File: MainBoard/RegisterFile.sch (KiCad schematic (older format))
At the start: 4 parts, among them U53 IDT7024L15PFG, U54 IDT7024L15PFG

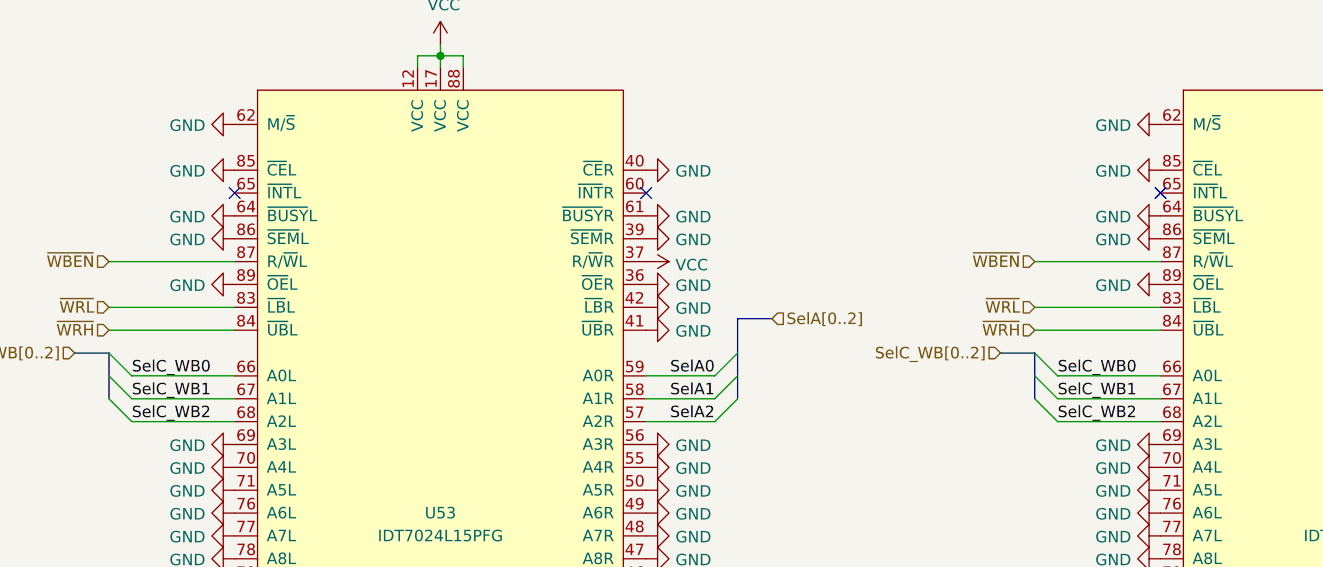
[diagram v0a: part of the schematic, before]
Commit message: Fix incorrectly wired control signals in register file write port.
The left sides of the register file's two dual port SRAMs were being set to
output their values. We never want these ports to output their values. This
is the register file write port.
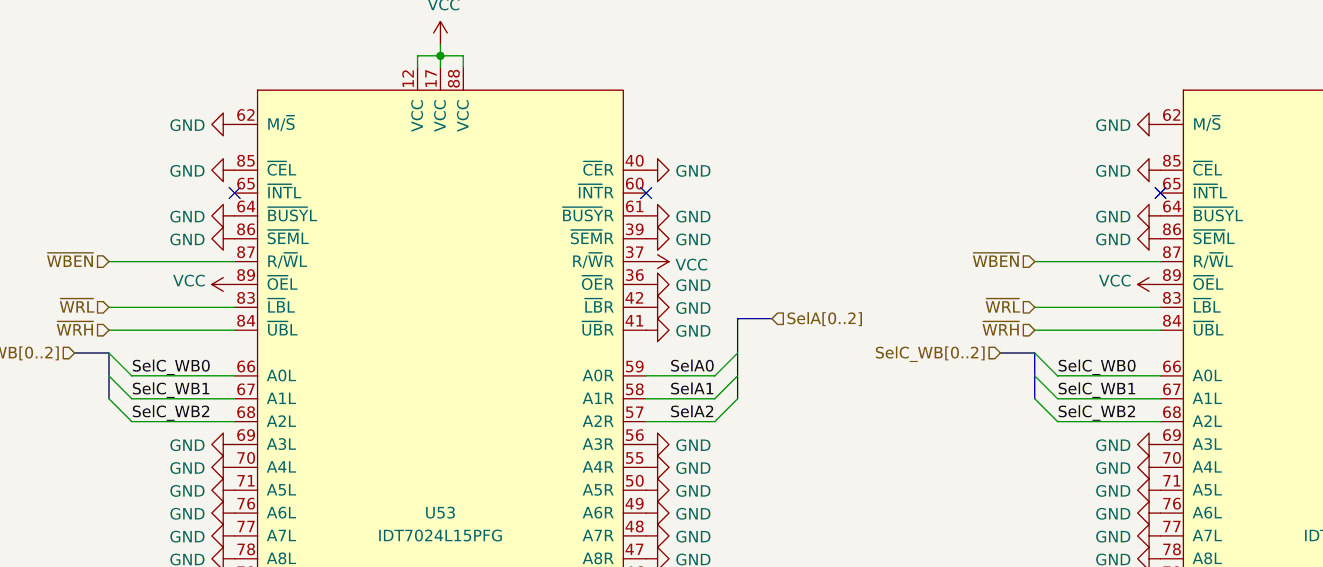
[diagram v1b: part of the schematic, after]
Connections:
- net GND: no longer U53.89 (~OE~L), U54.89 (~OE~L)
- net VCC: now also U53.89 (~OE~L), U54.89 (~OE~L)
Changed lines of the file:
@@
-$EndComp
-$Comp
-L power:GND #PWR0303
-U 1 1 5FD4C82D
-P 2550 2600
-F 0 "#PWR0303" H 2550 2350 50  0001 C CNN
-F 1 "GND" V 2555 2472 50  0000 R CNN
-F 2 "" H 2550 2600 50  0001 C CNN
-F 3 "" H 2550 2600 50  0001 C CNN
-	1    2550 2600
-	0    1    1    0
 $EndComp
 $Comp
@@
 $EndComp
 $Comp
-L power:GND #PWR0335
-U 1 1 5FDF3581
-P 6600 2600
-F 0 "#PWR0335" H 6600 2350 50  0001 C CNN
-F 1 "GND" V 6605 2472 50  0000 R CNN
-F 2 "" H 6600 2600 50  0001 C CNN
-F 3 "" H 6600 2600 50  0001 C CNN
-	1    6600 2600
-	0    1    1    0
-$EndComp
-$Comp
 L power:GND #PWR0347
 U 1 1 5FDF358D
@@
 Wire Bus Line
 	8800 4200 8800 5700
+$Comp
+L power:VCC #PWR?
+U 1 1 6061B77C
+P 2550 2600
+F 0 "#PWR?" H 2550 2450 50  0001 C CNN
+F 1 "VCC" V 2565 2727 50  0000 L CNN
+F 2 "" H 2550 2600 50  0001 C CNN
+F 3 "" H 2550 2600 50  0001 C CNN
+	1    2550 2600
+	0    -1   -1   0
+$EndComp
+$Comp
+L power:VCC #PWR?
+U 1 1 6061C045
+P 6600 2600
+F 0 "#PWR?" H 6600 2450 50  0001 C CNN
+F 1 "VCC" V 6615 2727 50  0000 L CNN
+F 2 "" H 6600 2600 50  0001 C CNN
+F 3 "" H 6600 2600 50  0001 C CNN
+	1    6600 2600
+	0    -1   -1   0
+$EndComp
 $EndSCHEMATC

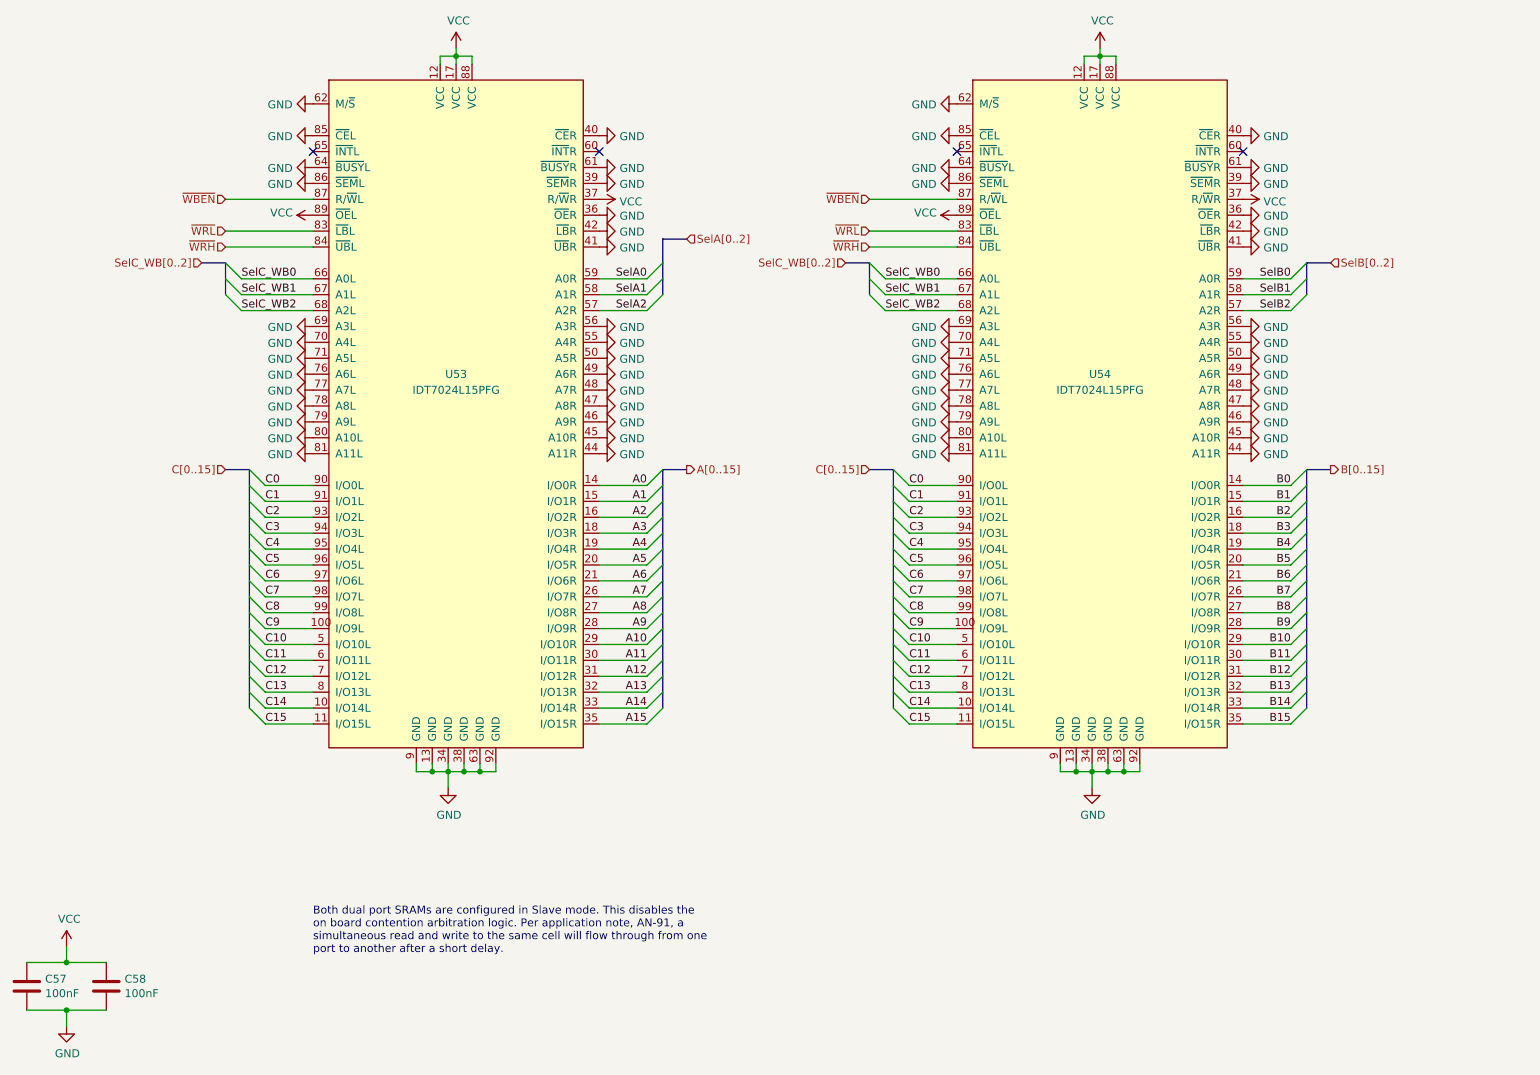
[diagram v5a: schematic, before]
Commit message: Add hazard control logic to ID.
TODO: The simulator has not been updated.
TODO: Hardware for operand forwarding has not been added yet.
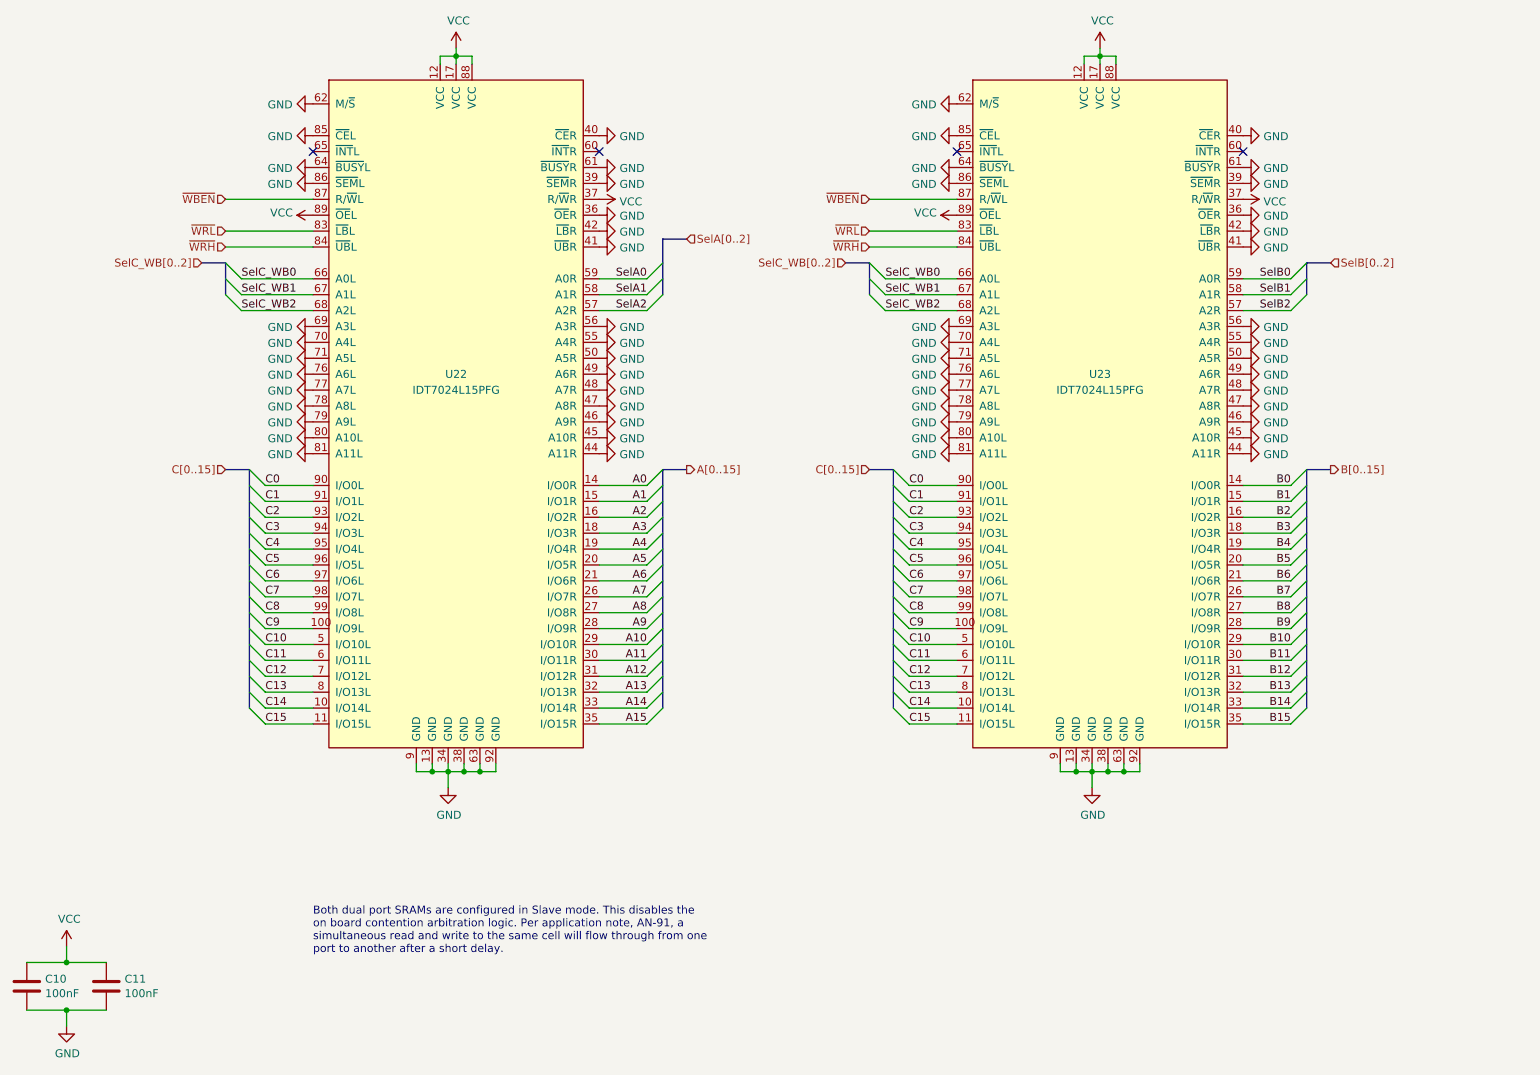
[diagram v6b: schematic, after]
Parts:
- renumbered U53 to U22, U54 to U23

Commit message: Add hardware for operand forwarding, and place on the PCB.
Resolve RAW hazards by forwarding results from a subsequent pipeline stage.

TODO: The simulator has not been updated yet.
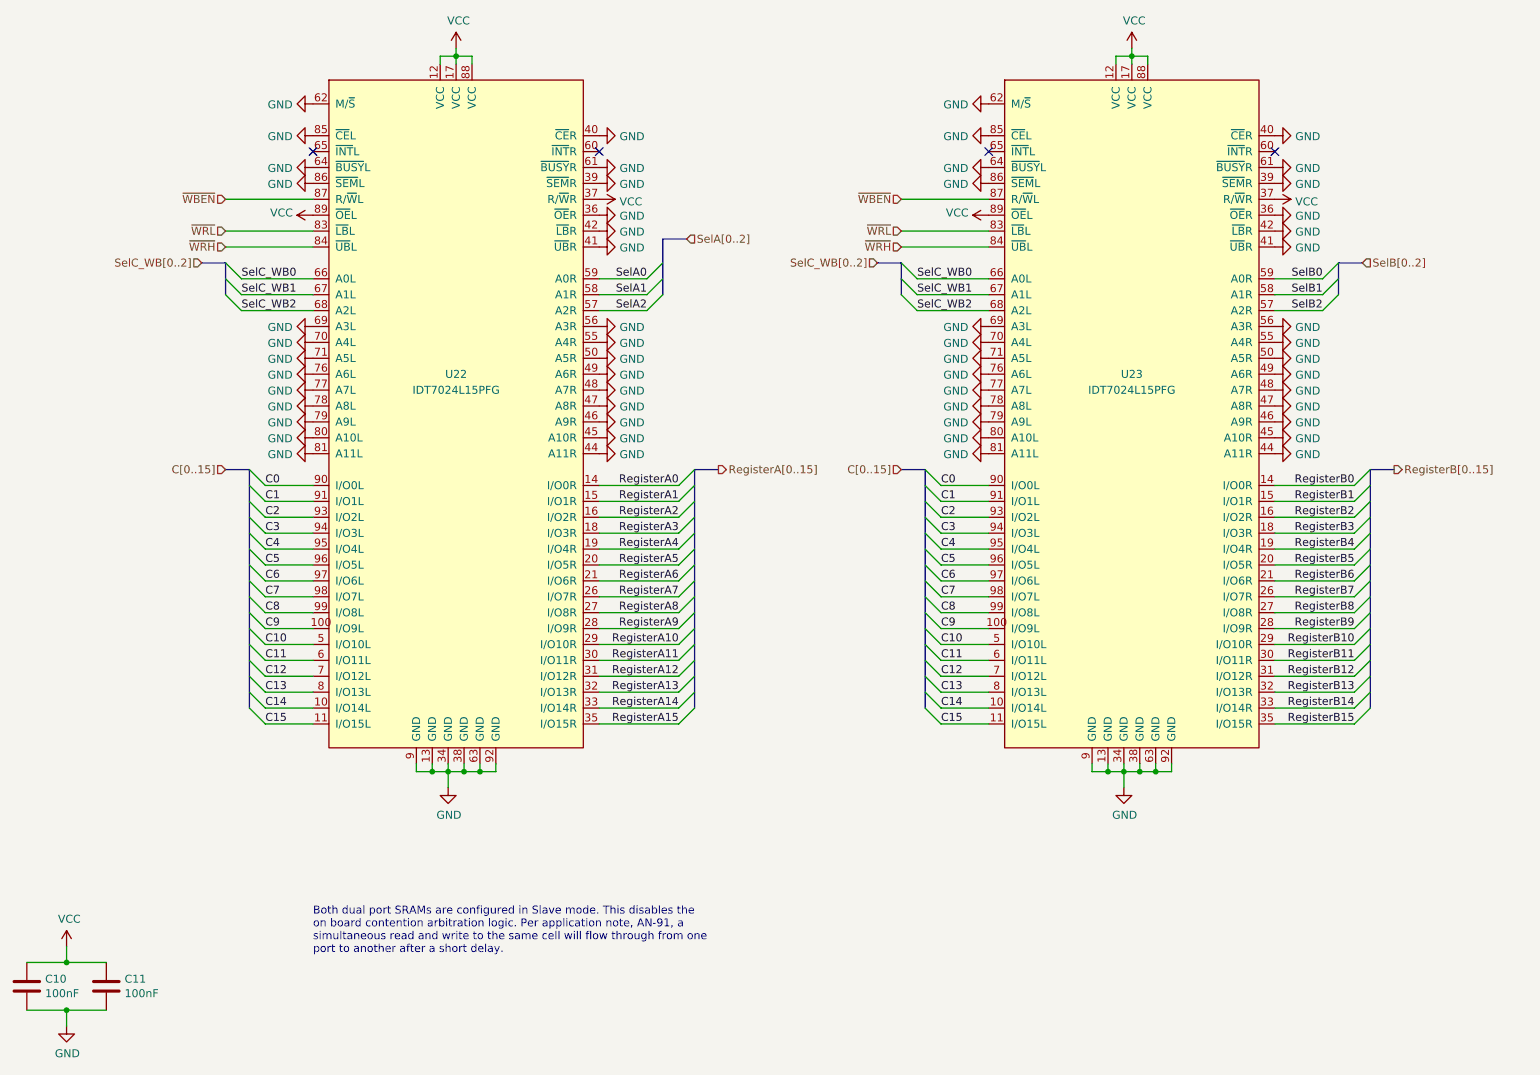
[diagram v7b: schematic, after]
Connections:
- net A0 renamed RegisterA0
- net A1 renamed RegisterA1
- net A10 renamed RegisterA10
- net A11 renamed RegisterA11
- net A12 renamed RegisterA12
- net A13 renamed RegisterA13
- net A14 renamed RegisterA14
- net A15 renamed RegisterA15
- net A2 renamed RegisterA2
- net A3 renamed RegisterA3
- net A4 renamed RegisterA4
- net A5 renamed RegisterA5
- net A6 renamed RegisterA6
- net A7 renamed RegisterA7
- net A8 renamed RegisterA8
- net A9 renamed RegisterA9
- net B0 renamed RegisterB0
- net B1 renamed RegisterB1
- net B10 renamed RegisterB10
- net B11 renamed RegisterB11
- net B12 renamed RegisterB12
- net B13 renamed RegisterB13
- net B14 renamed RegisterB14
- net B15 renamed RegisterB15
- net B2 renamed RegisterB2
- net B3 renamed RegisterB3
- net B4 renamed RegisterB4
- net B5 renamed RegisterB5
- net B6 renamed RegisterB6
- net B7 renamed RegisterB7
- net B8 renamed RegisterB8
- net B9 renamed RegisterB9
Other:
- moved on the sheet: U23
